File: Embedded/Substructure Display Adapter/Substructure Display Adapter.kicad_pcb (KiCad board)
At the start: 2 copper layers, 9 parts, among them J1 HUB75, J2 Input, J3 Output, U1 D0 FFC, U2 74HC245D_653, U3 74HC245D_653

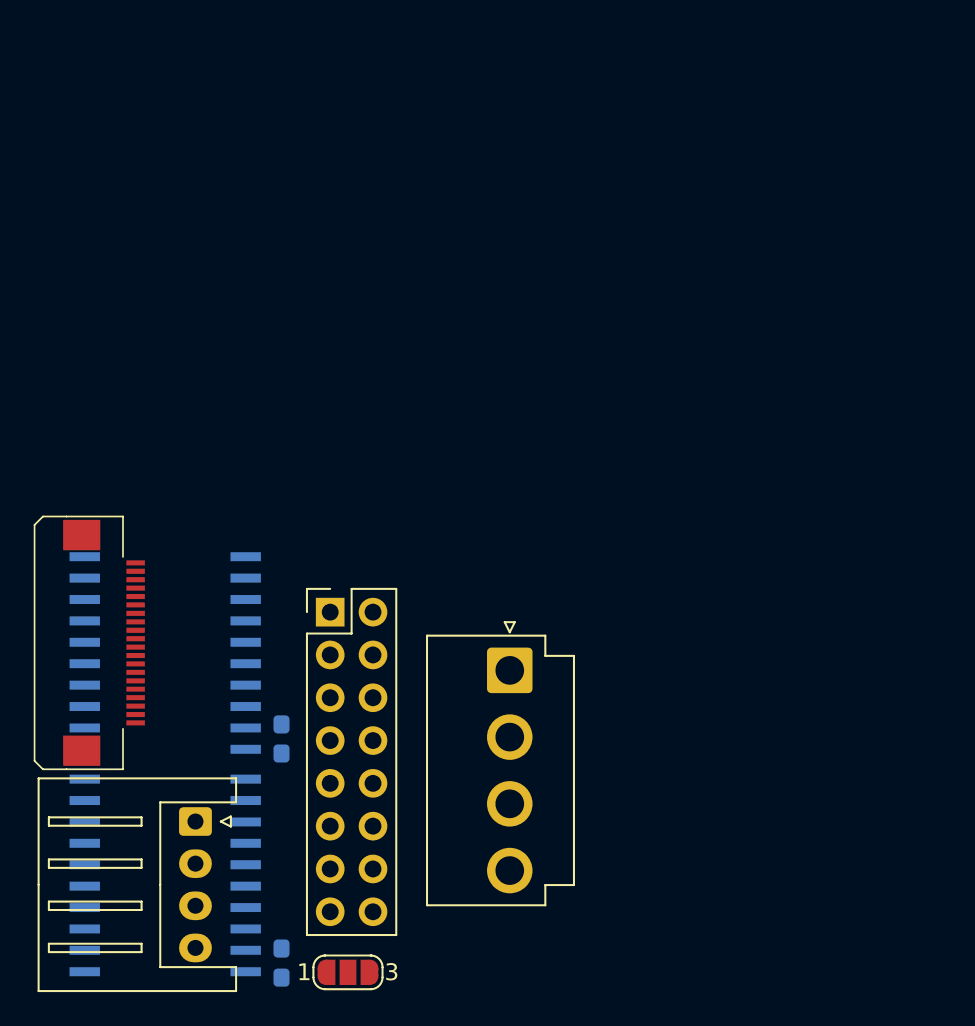
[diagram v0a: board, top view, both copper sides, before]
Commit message: Added PCB Routing
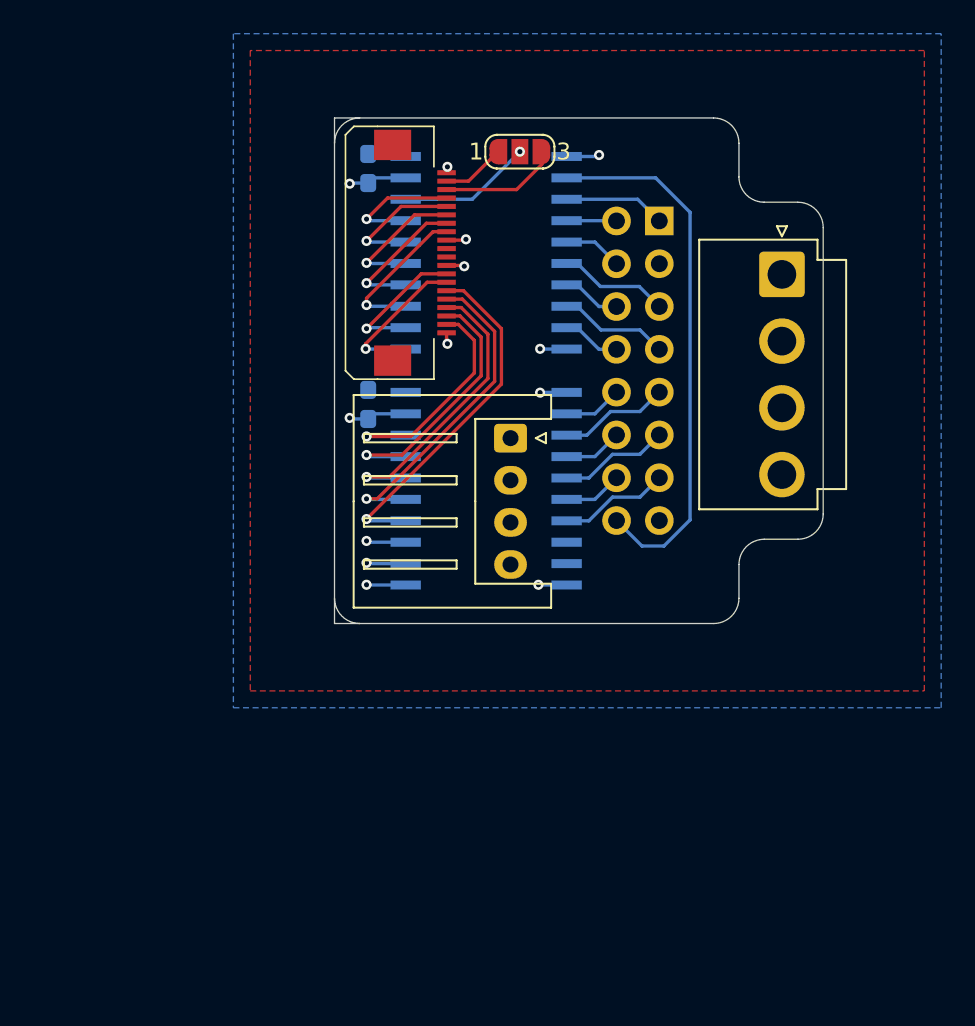
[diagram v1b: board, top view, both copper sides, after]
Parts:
- J1: moved to B.Cu
- moved JP1 49.8 mm to (117.0, 57.0)
- moved C1 34.2 mm to (108.0, 58.0), turned to -90 degrees
- moved C2 33.5 mm to (108.0, 72.0), turned to -90 degrees
- moved U2 30.4 mm to (115.0, 63.0), turned to 180 degrees
- moved J1 30.3 mm to (125.3, 61.1), turned to 180 degrees
- moved U3 29.8 mm to (115.0, 77.0), turned to 180 degrees
- moved U1 29.6 mm to (112.0, 63.0)
- moved J2 29.4 mm to (116.4, 74.0)
- moved J3 28.5 mm to (132.6, 64.3)
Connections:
- J1 pad 1: R0 -> G0
- J1 pad 10: B -> A
- J1 pad 11: C -> D
- J1 pad 12: D -> C
- J1 pad 13: CLK -> LAT
- J1 pad 14: LAT -> CLK
- J1 pad 15: OE -> GND
- J1 pad 16: GND -> OE
- J1 pad 2: G0 -> R0
- J1 pad 3: B0 -> GND
- J1 pad 4: GND -> B0
- J1 pad 5: R1 -> G1
- J1 pad 6: G1 -> R1
- J1 pad 7: B1 -> E
- J1 pad 8: E -> B1
- J1 pad 9: A -> B
- JP1 pad 1: unconnected-(JP1-A-Pad1) -> Disp GPIO 0
- JP1 pad 3: unconnected-(JP1-B-Pad3) -> Disp GPIO 1
- U2 pad 1: +5V -> GND
- U2 pad 11: unconnected-(U2-B7-Pad11) -> Disp GPIO 10
- U2 pad 12: unconnected-(U2-B6-Pad12) -> Disp GPIO 9
- U2 pad 13: unconnected-(U2-B5-Pad13) -> Disp GPIO 6
- U2 pad 14: unconnected-(U2-B4-Pad14) -> Disp GPIO 5
- U2 pad 15: unconnected-(U2-B3-Pad15) -> Disp GPIO 4
- U2 pad 16: unconnected-(U2-B2-Pad16) -> Disp GPIO 3
- U2 pad 17: unconnected-(U2-B1-Pad17) -> Disp GPIO 2
- U2 pad 18: unconnected-(U2-B0-Pad18) -> Disp Display Select
- U2 pad 2: unconnected-(U2-A0-Pad2) -> OE
- U2 pad 3: unconnected-(U2-A1-Pad3) -> G0
- U2 pad 4: unconnected-(U2-A2-Pad4) -> R0
- U2 pad 5: unconnected-(U2-A3-Pad5) -> B0
- U2 pad 6: unconnected-(U2-A4-Pad6) -> G1
- U2 pad 7: unconnected-(U2-A5-Pad7) -> R1
- U2 pad 8: unconnected-(U2-A6-Pad8) -> E
- U2 pad 9: unconnected-(U2-A7-Pad9) -> B1
- U3 pad 1: +5V -> GND
- U3 pad 14: unconnected-(U3-B4-Pad14) -> Disp GPIO 11
- U3 pad 15: unconnected-(U3-B3-Pad15) -> Disp GPIO 12
- U3 pad 16: unconnected-(U3-B2-Pad16) -> Disp GPIO 13
- U3 pad 17: unconnected-(U3-B1-Pad17) -> Disp GPIO 14
- U3 pad 18: unconnected-(U3-B0-Pad18) -> Disp GPIO 15
- U3 pad 2: unconnected-(U3-A0-Pad2) -> A
- U3 pad 3: unconnected-(U3-A1-Pad3) -> B
- U3 pad 4: unconnected-(U3-A2-Pad4) -> C
- U3 pad 5: unconnected-(U3-A3-Pad5) -> D
- U3 pad 6: unconnected-(U3-A4-Pad6) -> CLK
- U3 pad 7: unconnected-(U3-A5-Pad7) -> LAT
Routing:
- net OE: track 0.00 -> 32.1 mm
- net Disp GPIO 11: track 0.00 -> 21.2 mm, vias 0 -> 1
- net Disp GPIO 12: track 0.00 -> 19.4 mm, vias 0 -> 1
- net Disp GPIO 13: track 0.00 -> 17.7 mm, vias 0 -> 1
- net Disp GPIO 14: track 0.00 -> 16.0 mm, vias 0 -> 1
- net GND: track 0.00 -> 14.8 mm, vias 0 -> 8
- net Disp GPIO 15: track 0.00 -> 14.3 mm, vias 0 -> 1
- net Disp GPIO 6: track 0.00 -> 9.14 mm, vias 0 -> 1
- net Disp GPIO 10: track 0.00 -> 8.99 mm, vias 0 -> 1
- net Disp GPIO 5: track 0.00 -> 8.59 mm, vias 0 -> 1
- net Disp GPIO 9: track 0.00 -> 8.44 mm, vias 0 -> 1
- net Disp GPIO 4: track 0.00 -> 8.27 mm, vias 0 -> 1
- net Disp GPIO 3: track 0.00 -> 7.95 mm, vias 0 -> 1
- net Disp Display Select: track 0.00 -> 7.95 mm, vias 0 -> 1
- net Disp GPIO 2: track 0.00 -> 7.63 mm, vias 0 -> 1
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- added copper zone on B.Cu, net +5V
- added copper zone on F.Cu, net GND
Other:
- board outline added: 29 x 30 mm
